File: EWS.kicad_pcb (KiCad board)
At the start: 4 copper layers, 65 x 56 mm, 101 parts, among them J301 GPIO, J302 FAN, J401 PWR IN, J402 Toolhead 1, J403 Toolhead 2, J404 XH, J405 IN, J406 OUT, J407 OUT, Q301 AO3400A, Q401 CJAC70P06, SW301 BOOT0, SW302 RST, U201 XC6206PxxxMR, U202 XR76208, U301 STM32G0B1KBUx, U401 TJA1051TK-3, U402 CH334F, U403 USBLC6-2SC6, U404 USBLC6-2SC6, U405 USBLC6-2SC6

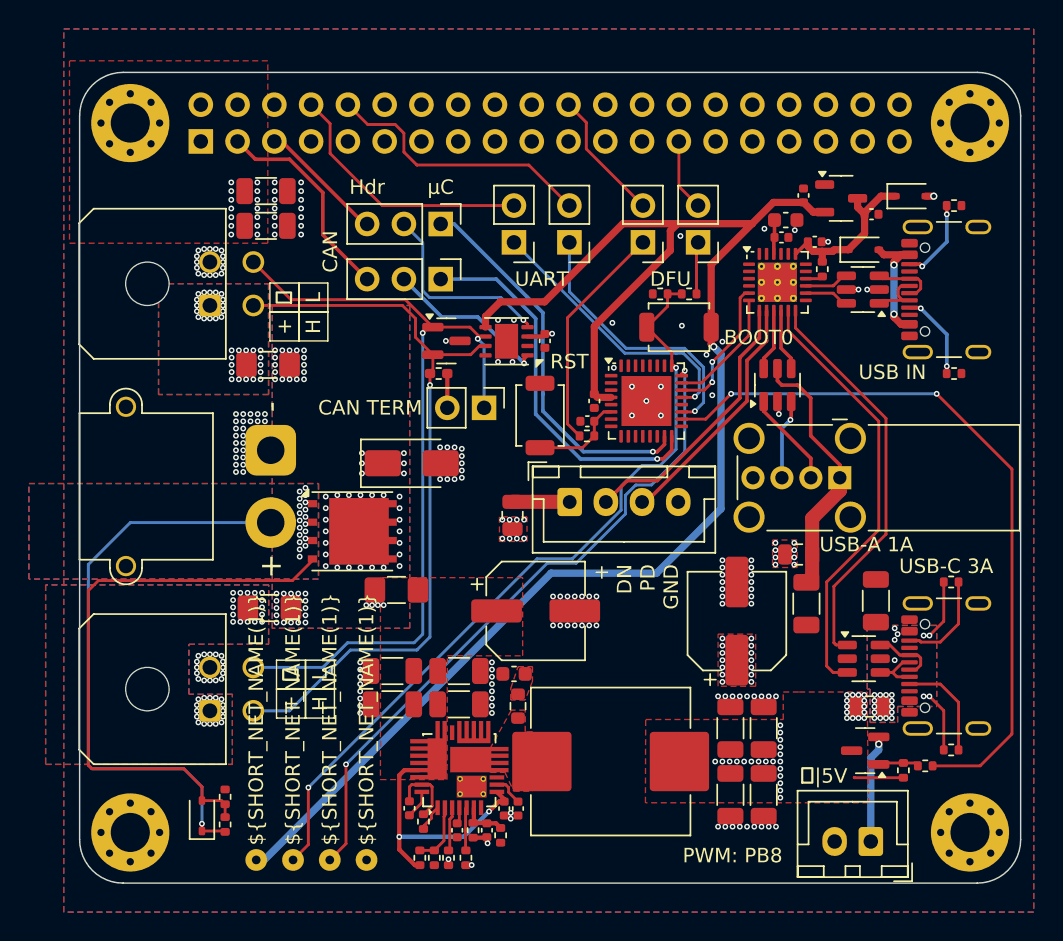
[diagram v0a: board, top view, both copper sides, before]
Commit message: Major hardware update: toolhead switching, DC/DC protection, and documentation overhaul
Hardware Changes:
- Replaced reverse polarity protection with 2x PFET toolhead switching (PB2/PA5 control)
- Added SS56 Schottky diode reverse polarity protection for DC/DC converter
- Updated current limit resistor to 5.1kΩ (~10.2A)
- Removed fan control circuitry and JST-XH connector
- Removed internal JST-XH USB port with fuse/protection

Documentation Updates:
- Updated both README files to reflect hardware changes
- Removed all fan control references and configurations
- Updated Klipper configuration examples
- Cleaned up pinout and connector assignments
- Updated technical specifications table
- Fixed table of contents and cross-references
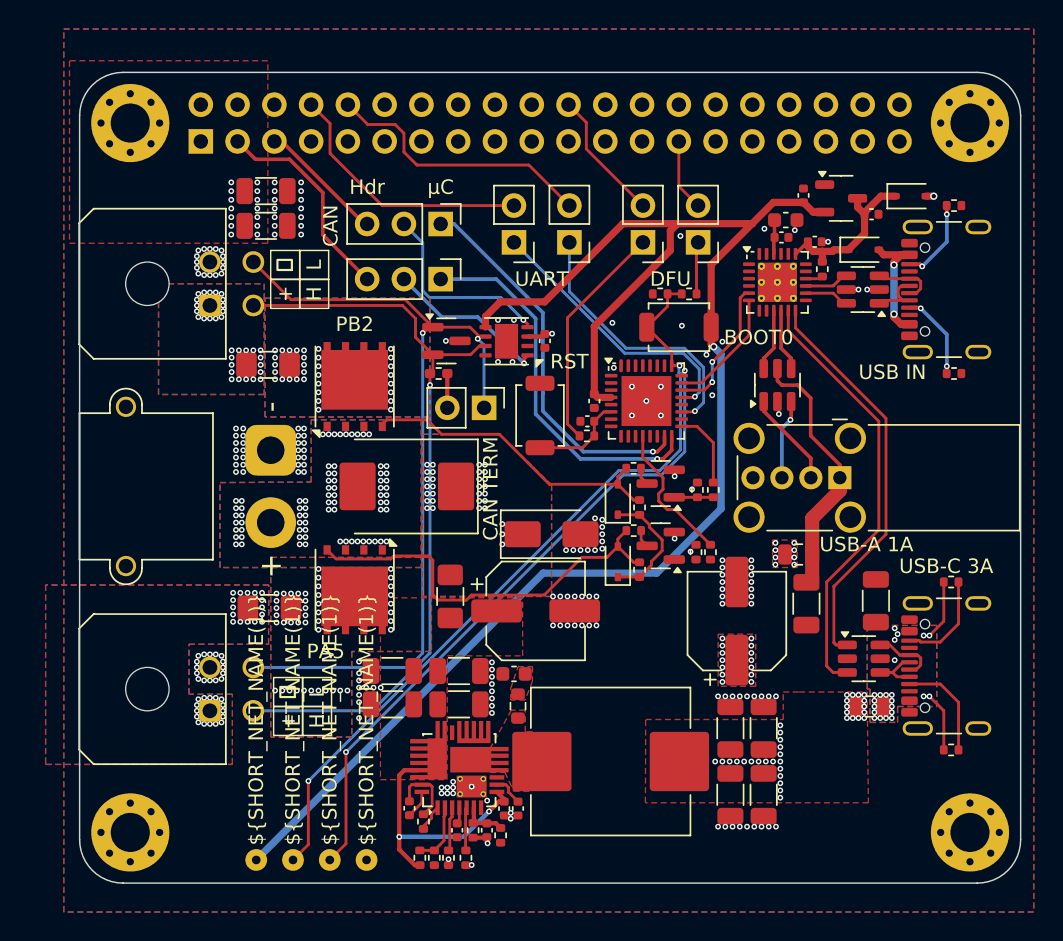
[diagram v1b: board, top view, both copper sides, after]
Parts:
- removed F405: 1.5A, Fuse:Fuse_0805_2012Metric
- removed J302: FAN, Connector_JST:JST_XH_B2B-XH-A_1x02_P2.50mm_Vertical
- removed J404: XH, Connector_JST:JST_XH_B4B-XH-A_1x04_P2.50mm_Vertical
- removed Q301: AO3400A, Package_TO_SOT_SMD:SOT-23
- removed R304: 1k, Resistor_SMD:R_0402_1005Metric
- removed R305: 10k, Resistor_SMD:R_0402_1005Metric
- removed R402: 30k, Resistor_SMD:R_0402_1005Metric
- removed the REF** at (173.1, 86.8)
- removed the REF** at (173.5, 90.0)
- added D402: D_Schottky, Diode_SMD:D_SMC, F.Cu at (152.6, 95.6)
- added D407: BZT52C15S, Diode_SMD:D_SOD-323, F.Cu at (167.2, 100.8)
- added Q403: AO3400A, Package_TO_SOT_SMD:SOT-23, F.Cu at (170.1, 95.4)
- added Q404: CJAC70P06, Package_DFN_QFN:AO_DFN-8-1EP_5.55x5.2mm_P1.27mm_EP4.12x4.6mm, F.Cu at (149.0, 102.7)
- added Q405: AO3400A, Package_TO_SOT_SMD:SOT-23, F.Cu at (170.1, 99.7)
- added R403: 30k, Resistor_SMD:R_0402_1005Metric, F.Cu at (168.3, 94.3)
- added R406: 30k, Resistor_SMD:R_0402_1005Metric, F.Cu at (172.7, 95.8)
- added R407: 1k, Resistor_SMD:R_0402_1005Metric, F.Cu at (173.8, 95.8)
- added R413: 30k, Resistor_SMD:R_0402_1005Metric, F.Cu at (168.7, 101.3)
- added R414: 30k, Resistor_SMD:R_0402_1005Metric, F.Cu at (168.3, 98.7)
- added R415: 30k, Resistor_SMD:R_0402_1005Metric, F.Cu at (172.6, 100.1)
- added R416: 1k, Resistor_SMD:R_0402_1005Metric, F.Cu at (173.6, 100.1)
- moved D401 36.1 mm to (167.2, 96.5)
- moved R401 36.0 mm to (168.7, 97.0)
- moved D403 10.8 mm to (162.6, 98.9)
- moved Q401 10.0 mm to (149.0, 88.7), turned to 90 degrees
- moved F201 3.74 mm to (155.6, 103.2), turned to 90 degrees
- renumbered D402 to D404, D404 to D406, MH1 to MH101, MH2 to MH102, MH3 to MH103, MH4 to MH104, R208 to R202, R202 to R203, R203 to R204, R204 to R205, R205 to R206, R206 to R207, R207 to R208, R303 to R301, R301 to R302, R302 to R303, R403 to R405, R404 to R408, R405 to R409, R406 to R410, R407 to R411, R408 to R412, SW302 to SW301, SW301 to SW302, TP302 to TP301, TP301 to TP302
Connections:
- net /Connectivity/GATE renamed /Connectivity/HE GATE 2
- F401 pad 1: 24V -> /Connectivity/OUT1
- F401 pad 2: /Connectivity/OUT1 -> /Connectivity/OUT1F
- F402 pad 1: 24V -> /Connectivity/OUT2
- F402 pad 2: /Connectivity/OUT2 -> /Connectivity/OUT2F
- J402 pad 1: /Connectivity/OUT1 -> /Connectivity/OUT1F
- J403 pad 1: /Connectivity/OUT2 -> /Connectivity/OUT2F
- Q401 pad 5: 24V -> /Connectivity/OUT2
- U301 pad 12: unconnected-(U301-PA5-Pad12) -> HE1 ON
- U301 pad 17: unconnected-(U301-PB2-Pad17) -> HE2 ON
- U301 pad 18: Net-(U301-PA8) -> unconnected-(U301-PA8-Pad18)
- U402 pad 7: Net-(J404-Pin_2) -> unconnected-(U402-DM3-Pad7)
- U402 pad 8: Net-(J404-Pin_3) -> unconnected-(U402-DP3-Pad8)
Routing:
- net Net-(U301-PA8): track 50.4 -> 0.00 mm, vias 2 -> 0
- net /Connectivity/VEXT: track 40.8 -> 8.60 mm, vias 20 -> 74
- net /Connectivity/HE GATE 1: track 0.00 -> 27.9 mm
- net /Connectivity/HE GATE 2: track 40.5 -> 21.7 mm
- net Net-(J404-Pin_2): track 18.8 -> 0.00 mm
- net Net-(J404-Pin_3): track 16.9 -> 0.00 mm
- net HE1 ON: track 0.00 -> 10.0 mm
- net Net-(J302-Pin_1): track 7.45 -> 0.00 mm, vias 1 -> 0
- net HE2 ON: track 0.00 -> 5.41 mm
- net Net-(J404-Pin_1): track 3.96 -> 0.00 mm
- net 5V: track 8.39 -> 4.98 mm, vias 83 -> 75
- net Net-(Q301-G): track 2.82 -> 0.00 mm
- net Net-(Q403-G): track 0.00 -> 2.70 mm
- net Net-(Q403-D): track 0.00 -> 1.23 mm
- net Net-(Q405-D): track 0.00 -> 1.22 mm
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- added copper zone on B.Cu, net /Connectivity/OUT1F
- added copper zone on F.Cu, net /Connectivity/OUT1F
- added copper zone on B.Cu, net /Connectivity/OUT2F
- added copper zone on F.Cu, net /Connectivity/OUT2F
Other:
- board text added: "PA5"
- board text added: "PB2"
- board text removed: "+ DN PD GND"
- board text removed: "PWM: PB8"
- board text removed: "⏚|5V"

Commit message: Enhanced documentation and final hardware corrections
Documentation Improvements:
- Added comprehensive 'Problems Addressed' section explaining the value proposition
- Covers power supply issues, CAN communication problems, safety concerns, and wiring challenges
- Removed JST-XH internal USB port references from pinout sections
- Corrected via placement specification (DC/DC PGND instead of output)

Hardware Updates:
- Updated schema files with latest component changes
- Added custom footprints for XR76203ELTR-F and heat sink components
- Refined manufacturing guidelines for optimal thermal performance

The documentation now clearly articulates the EWS board's role in solving common
Voron 3D printer control system challenges.
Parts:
- added NT201: NetTie_2, NetTie:NetTie-2_SMD_Pad0.5mm, F.Cu at (156.1, 116.2)
- added REF**: HeatSink_9x9x5, project:HeatSink_9x9x5, B.Cu at (157.2, 112.2)
- R205: value 5k6 -> 5k1
- moved REF** 34.4 mm to (190.9, 100.8), turned to 90 degrees
- moved QR***** 1.54 mm to (172.8, 111.3)
- moved R205 0.51 mm to (154.2, 119.0), turned to 0 degrees
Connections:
- net Net-(J301-Pin_3) renamed /MCU/SOC CAN TX
- net Net-(J301-Pin_5) renamed /MCU/SOC CAN RX
- C209 pad 2: GND -> /Power/AGND
- C210 pad 2: GND -> /Power/AGND
- R204 pad 2: GND -> /Power/AGND
- R208 pad 2: GND -> /Power/AGND
- U202 pad 10: GND -> /Power/AGND
- U202 pad 7: GND -> /Power/AGND
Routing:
- net Net-(C211-Pad2): track 4.82 -> 5.61 mm
- net Net-(U202-I_{LIM}): track 1.86 -> 1.22 mm
- net GND: vias 186 -> 187
- net /Power/AGND: vias 0 -> 6
- added copper zone on F.Cu, net /Power/AGND
- added copper zone on In1.Cu, net /Power/AGND

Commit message: EWS Rev 0.1 - Complete design with documentation
Release Features:
- Universal HAT for Raspberry Pi 4/5 and Radxa Rock 5B/5B+
- 8A DC/DC converter with SS56 reverse polarity protection
- Dual toolhead switching via PFETs (PB2/PA5 control)
- Native CAN and USB-CAN bridge support
- USB hub with power delivery for touchscreens
- Comprehensive safety features and thermal management

Hardware:
- STM32G0B1KBU6 MCU with crystal-less design
- MaxLinear XR76208 switching regulator
- MCP2542WFD CAN transceiver with jumper selection
- WCH CH334F USB hub with MTT support
- 2oz copper PCB recommended for thermal performance

Documentation:
- Bilingual documentation (German/English)
- Installation guides with kernel diagnostics
- Klipper configuration examples
- Comprehensive problem statement and solutions
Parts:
- added REF**: EduardIten, project:EduardIten, B.Cu at (138.7, 93.5)
- added REF**: EWS Rev. 1.0, project:EWS Rev. 1.0, B.Cu at (135.9, 93.8)

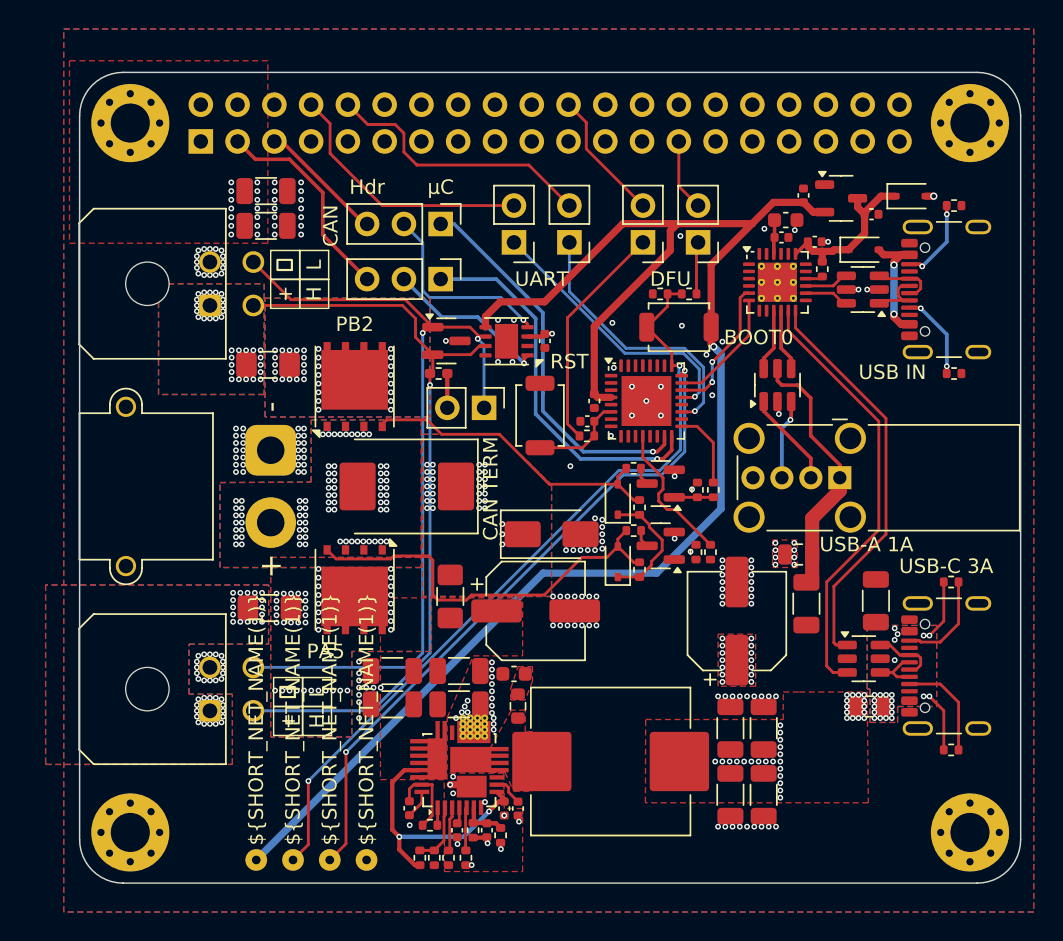
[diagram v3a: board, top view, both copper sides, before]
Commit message: Rev 0.2: Major hardware improvements and production readiness
Hardware Improvements (Thanks to shx for schematic cleanup):
- Clean up schematic organization and structure
- Set CAN transceiver Silent pin to GND for stability
- Add status LEDs (yellow: 24V/5V/3.3V, green: MCU PB4)
- Replace jumpers with solder jumpers on bottom side
- Add jumpers to output PFETs for permanent-on without firmware
- Add robust test points for 5V/GND load testing
- Add optional heatsink for DC/DC converter on bottom
- Add 10µF capacitor for MCU on 3.3V rail

Component Optimizations:
- Replace 30kΩ with 33kΩ basic part for simplified BOM
- Change DC/DC feedback: 15.5kΩ15kΩ (new output: 5.1V)
- Upgrade CAN ESD protection: NUP2105LPESD1CAN
- Increase CAN termination resistor footprint: 04020603
- Switch USB hub supply from 5V to 3.3V per datasheet

Production Ready:
- Add all LCSC part numbers and rotations
- Generate complete production data package
- Improve PCB layout and button placement
- Create comprehensive changelog documentation
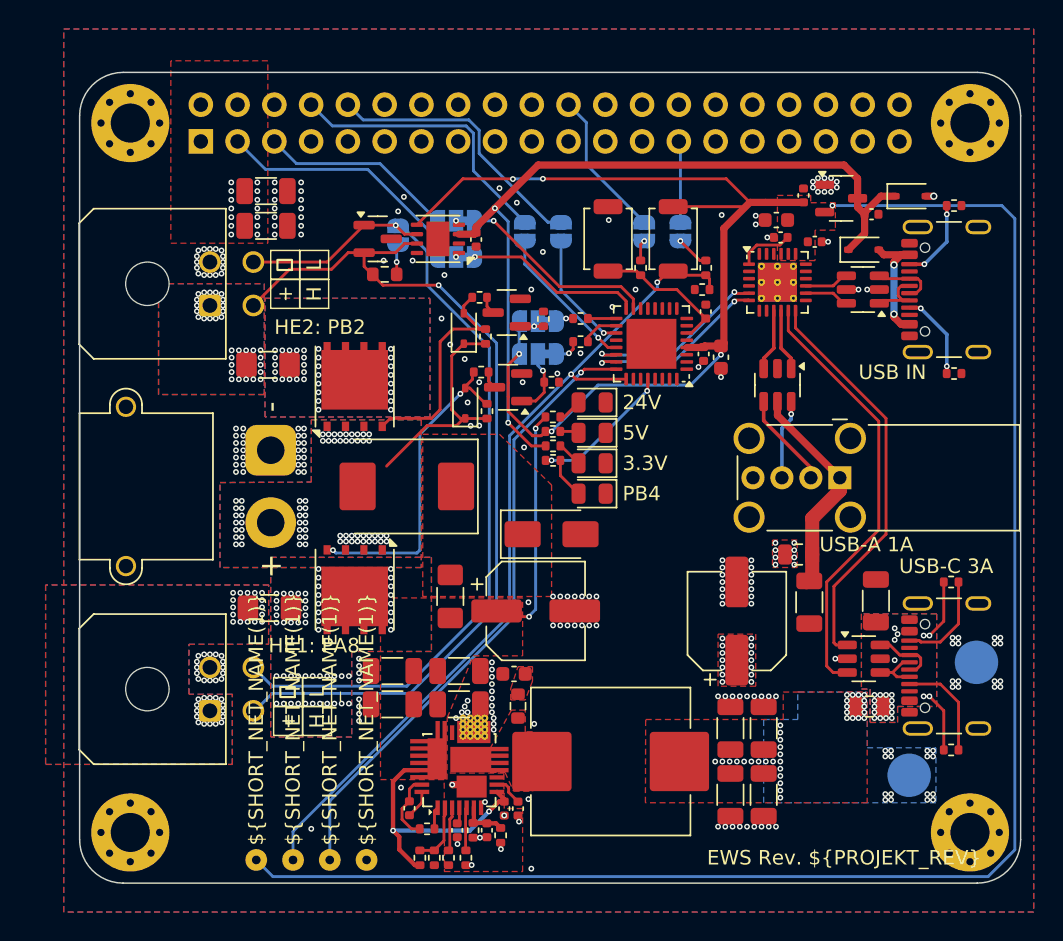
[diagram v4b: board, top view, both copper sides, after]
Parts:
- removed QR*****: http://github.com/eiten/EWS, project:http___github.com_eiten_EWS
- removed R416: 1k, Resistor_SMD:R_0402_1005Metric
- removed REF**: CC_BY_NC_SA 4, project:CC_BY_NC_SA 4
- removed REF**: EduardIten, project:EduardIten
- removed REF**: EWS Rev. 1.0, project:EWS Rev. 1.0
- removed REF**: HeatSink_9x9x5, project:HeatSink_9x9x5
- added C303: 10u, Capacitor_SMD:C_0603_1608Metric, F.Cu at (174.3, 86.7)
- added D201: YELLOW, LED_SMD:LED_0805_2012Metric, F.Cu at (165.4, 89.8)
- added D202: YELLOW, LED_SMD:LED_0805_2012Metric, F.Cu at (165.4, 94.0)
- added D203: YELLOW, LED_SMD:LED_0805_2012Metric, F.Cu at (165.4, 91.9)
- added D301: GREEN, LED_SMD:LED_0805_2012Metric, F.Cu at (165.4, 96.1)
- added HS201: Heatsink, project:HeatSink_9x9x5, B.Cu at (157.2, 112.2)
- added JP401: ~, project:SolderJumper-3_P1.3mm_Bridged12_RoundedPad1.0x1.5mm_custom, B.Cu at (161.7, 86.4)
- added JP402: ~, project:SolderJumper-3_P1.3mm_Bridged12_RoundedPad1.0x1.5mm_custom, B.Cu at (161.7, 84.2)
- added LABEL101: PCB NAME, project:EWS Rev. 1.0, B.Cu at (139.0, 98.0)
- added LABEL102: CREATED BY, project:EduardIten, B.Cu at (136.4, 98.5)
- added LABEL103: https://github.com/eiten/EWS, project:http___github.com_eiten_EWS, B.Cu at (174.5, 111.8)
- added LABEL104: LICENSE, project:CC_BY_NC_SA 4, B.Cu at (190.8, 100.8)
- added LABEL105: SWITZERLAND, project:Switzerland, B.Cu at (151.5, 94.7)
- added R201: 22k, Resistor_SMD:R_0402_1005Metric, F.Cu at (162.7, 90.8)
- added R202: 2k2, Resistor_SMD:R_0402_1005Metric, F.Cu at (162.7, 92.8)
- added R203: 1k, Resistor_SMD:R_0402_1005Metric, F.Cu at (162.7, 91.8)
- added R301: 330R, Resistor_SMD:R_0402_1005Metric, F.Cu at (162.7, 93.8)
- added TP202: 5V, TestPoint:TestPoint_Pad_D3.0mm, B.Cu at (187.3, 115.5)
- added TP203: GND, TestPoint:TestPoint_Pad_D3.0mm, B.Cu at (191.9, 107.8)
- D302: renamed from D404; value NUP2105L -> PESD1CAN
- D403: renamed from D402; value D_Schottky -> SS56
- J401: value PWR IN -> XT30
- J402: value Toolhead 1 -> MX3.0 2x2
- J403: value Toolhead 2 -> MX3.0 2x2
- J404: renamed from J405; value IN -> USB-C
- J405: renamed from J406; value OUT -> USB-C
- J406: renamed from J407; value OUT -> USB-A
- JP301: renamed from JP306; value Jumper_3_Open -> ~; footprint Connector_PinHeader_2.54mm:PinHeader_1x03_P2.54mm_Vertical -> project:SolderJumper-3_P1.3mm_Bridged12_RoundedPad1.0x1.5mm_custom; moved to B.Cu
- JP302: renamed from JP301; value Jumper_3_Open -> ~; footprint Connector_PinHeader_2.54mm:PinHeader_1x03_P2.54mm_Vertical -> project:SolderJumper-3_P1.3mm_Bridged12_RoundedPad1.0x1.5mm_custom; moved to B.Cu
- JP303: renamed from JP401; footprint Connector_PinHeader_2.54mm:PinHeader_1x02_P2.54mm_Vertical -> Jumper:SolderJumper-2_P1.3mm_Open_RoundedPad1.0x1.5mm; moved to B.Cu
- JP304: renamed from JP302; footprint Connector_PinHeader_2.54mm:PinHeader_1x02_P2.54mm_Vertical -> Jumper:SolderJumper-2_P1.3mm_Open_RoundedPad1.0x1.5mm; moved to B.Cu
- JP305: renamed from JP303; footprint Connector_PinHeader_2.54mm:PinHeader_1x02_P2.54mm_Vertical -> Jumper:SolderJumper-2_P1.3mm_Open_RoundedPad1.0x1.5mm; moved to B.Cu
- JP306: renamed from JP304; footprint Connector_PinHeader_2.54mm:PinHeader_1x02_P2.54mm_Vertical -> Jumper:SolderJumper-2_P1.3mm_Open_RoundedPad1.0x1.5mm; moved to B.Cu
- JP307: renamed from JP305; footprint Connector_PinHeader_2.54mm:PinHeader_1x02_P2.54mm_Vertical -> Jumper:SolderJumper-2_P1.3mm_Open_RoundedPad1.0x1.5mm; moved to B.Cu
- R207: renamed from R204; value 30k -> 33k
- R210: renamed from R207; value 15.5k -> 15k
- R304: renamed from R405; footprint Resistor_SMD:R_0402_1005Metric_Pad0.72x0.64mm_HandSolder -> Resistor_SMD:R_0603_1608Metric
- R401: renamed from R413; value 30k -> 33k
- R402: renamed from R401; value 30k -> 33k
- R403: renamed from R414; value 30k -> 33k
- R404: renamed from R403; value 30k -> 33k
- R405: renamed from R415; value 30k -> 33k
- R406: value 30k -> 33k
- SW301: value RST -> TS-1088
- SW302: value BOOT0 -> TS-1088
- U201: value XC6206PxxxMR -> XC6206P332MR
- moved R408 17.0 mm to (164.6, 84.0), turned to 180 degrees
- moved D402 15.9 mm to (156.5, 84.7)
- moved R402 15.9 mm to (158.0, 85.2)
- moved R406 15.9 mm to (162.0, 84.0)
- moved Q404 15.9 mm to (159.5, 83.6)
- moved R404 15.9 mm to (157.6, 82.5)
- moved R405 15.4 mm to (162.6, 88.4), turned to 180 degrees
- moved D401 15.2 mm to (156.6, 89.8)
- moved R401 15.2 mm to (158.1, 90.4)
- moved Q403 15.2 mm to (159.6, 88.8)
- moved R403 15.2 mm to (157.7, 87.7)
- moved R407 13.7 mm to (164.6, 85.6), turned to 180 degrees
- moved JP303 13.3 mm to (152.0, 78.2)
- moved SW301 13.1 mm to (166.5, 78.5)
- moved R302 12.2 mm to (168.8, 80.5), turned to -90 degrees
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- renumbered C403 to C304, C303 to C305, C304 to C306, C405 to C403, C406 to C405, C407 to C406, D407 to D401, D401 to D402, D403 to D404, Q404 to Q401, Q401 to Q402, Q405 to Q403, Q403 to Q404, R201 to R204, R202 to R205, R203 to R206, R205 to R208, R206 to R209, R208 to R211, R301 to R302, R302 to R303, R303 to R305, R411 to R410, R412 to R411, R410 to R412, TP302 to TP201, TP303 to TP302, TP304 to TP303, U401 to U301, U301 to U302, U402 to U401, U403 to U402, U404 to U403, U405 to U404
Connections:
- net /Connectivity/CAN N renamed CAN L
- net /Connectivity/CAN P renamed CAN H
- net /Connectivity/HE GATE 1 renamed /Connectivity/HE1 GATE
- net /Connectivity/HE GATE 2 renamed /Connectivity/HE2 GATE
- net /Connectivity/VBUS COUT renamed Net-(U403-VBUS)
- net /Connectivity/VEXT renamed V_{EXT}
- net /MCU/SOC CAN RX renamed /MCU/SBC CAN RX
- net /MCU/SOC CAN TX renamed /MCU/SBC CAN TX
- net CAN_RX renamed Net-(JP301-C)
- net CAN_TX renamed Net-(JP302-C)
- C203 pad 2: 5VD -> 5V_{SYS}
- C304 pad 2: 5V -> 5V_{SYS}
- C401 pad 1: 5VD -> 3V3
- C402 pad 1: Net-(U402-VDD33) -> 3V3
- C404 pad 1: Net-(U402-VDD33) -> 3V3
- D405 pad 1: 5VD -> 5V_{SYS}
- D406 pad 1: 5VD -> 5V_{SYS}
- J404 pad A5: Net-(J405-CC1) (its old number) -> Net-(J404-CC1)
- J404 pad B5: Net-(J405-CC2) (its old number) -> Net-(J404-CC2)
- J406 pad 2: Net-(J407-D-) -> Net-(J406-D-)
- J406 pad 3: Net-(J407-D+) -> Net-(J406-D+)
- Q404 pad 1: Net-(Q403-G) -> Net-(JP402-C)
- R406 pad 2: Net-(Q403-G) -> Net-(JP402-C)
- R407 pad 1: Net-(Q403-G) -> HE1 ON
- R407 pad 2: HE2 ON -> Net-(JP401-A)
- R408 pad 1: Net-(U402-~{RESET}) -> HE2 ON
- R408 pad 2: 5VD -> Net-(JP402-A)
- R409 pad 1: GND -> Net-(J404-CC1)
- R409 pad 2: Net-(J405-CC1) (its old number) -> GND
- R410 pad 1: GND -> Net-(J404-CC2)
- R410 pad 2: Net-(J405-CC2) (its old number) -> GND
- U201 pad 3: 5VD -> 5V_{SYS}
- U301 pad 3: 5V -> 5V_{SYS}
- U301 pad 8: unconnected-(U401-S-Pad8) -> GND
- U302 pad 12: HE1 ON -> unconnected-(U302-PA5-Pad12)
- U302 pad 18: unconnected-(U301-PA8-Pad18) -> HE1 ON
- U302 pad 28: unconnected-(U301-PB4-Pad28) -> Net-(U302-PB4)
- U401 pad 1: unconnected-(U402-~{OVCUR}-Pad1) -> 3V3
- U401 pad 10: /Connectivity/USB A DP -> /Connectivity/USB A DN
- U401 pad 16: Net-(U402-~{RESET}) -> unconnected-(U401-~{RESET}-Pad16)
- U401 pad 18: GND -> unconnected-(U401-PSELF-Pad18)
- U401 pad 19: 5VD -> 3V3
- U401 pad 20: (no net) -> 3V3
- U401 pad 22: Net-(U402-VDD33) -> unconnected-(U401-LED1-Pad22)
- U401 pad 9: /Connectivity/USB A DN -> /Connectivity/USB A DP
- U404 pad 1: Net-(J407-D-) -> /Connectivity/USB A DN
- U404 pad 3: Net-(J407-D+) -> /Connectivity/USB A DP
- U404 pad 4: /Connectivity/USB A DP -> Net-(J406-D-)
- U404 pad 6: /Connectivity/USB A DN -> Net-(J406-D+)
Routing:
- net 3V3: track 106.4 -> 186.5 mm, vias 1 -> 6
- net 5V_{SYS}: track 0.00 -> 56.9 mm, vias 0 -> 2
- net /Power/VIN: track 18.0 -> 34.9 mm, vias 2 -> 4
- net Net-(JP304-A): track 15.9 -> 1.44 mm, vias 0 -> 1
- net /MCU/uC FDCAN1 TX: track 26.2 -> 12.2 mm
- net Net-(JP301-C): track 13.6 -> 0.36 mm
- net /MCU/uC FDCAN1 RX: track 26.7 -> 13.8 mm
- net 5VD: track 12.1 -> 0.00 mm
- net Net-(JP302-C): track 11.4 -> 0.36 mm
- net /MCU/uC USART TX: track 19.0 -> 8.43 mm
- net CAN H: track 53.0 -> 63.3 mm
- net Net-(U302-PB4): track 0.00 -> 9.83 mm, vias 0 -> 2
- net /MCU/uC USART RX: track 19.4 -> 10.3 mm
- net HE1 ON: track 10.0 -> 2.60 mm
- net V_{EXT}: track 8.60 -> 15.7 mm, vias 74 -> 64
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- added copper zone on F.Cu, net 3V3
- added copper zone on B.Cu, net 5V
- removed copper zone on B.Cu, net 24V
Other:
- board text added: "24V"
- board text added: "3.3V"
- board text added: "5V"
- board text added: "EWS Rev. ${PROJEKT_REV}"
- board text added: "HE1"
- board text added: "HE1: PA8"
- board text added: "HE2"
- board text added: "HE2: PB2"
- board text added: "ON"
- board text added: "PB4"
- board text added: "SBC"
- board text added: "TERM 120Ω"
- board text added: "~{RST}"
- board text removed: "CAN TERM"
- board text removed: "Hdr"
- board text removed: "PA5"
- board text removed: "PB2"
- board text removed: "RST"
